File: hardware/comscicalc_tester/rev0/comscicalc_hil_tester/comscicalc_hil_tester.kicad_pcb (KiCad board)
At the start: 4 copper layers, 106 x 61 mm, 116 parts, among them IC1 ADC088S022CIMTX_NOPB, IC2 74HC4052D,653, IC3 74HC4052D,653, IC4 74HC4052D,653, IC5 LM358ADGKR, J1 comscicalc_tester, J2 4-1734839-0, J3 Conn_02x12_Odd_Even, J4 Conn_01x04_Male, J5 Conn_01x02_Male, J6 USB4110-GF-A, Q1 DMG2301L, U1 MCP23017_SS, U2 TLV70033_SOT23-5, U3 RASPBERRY_PI_3_MODEL_B_

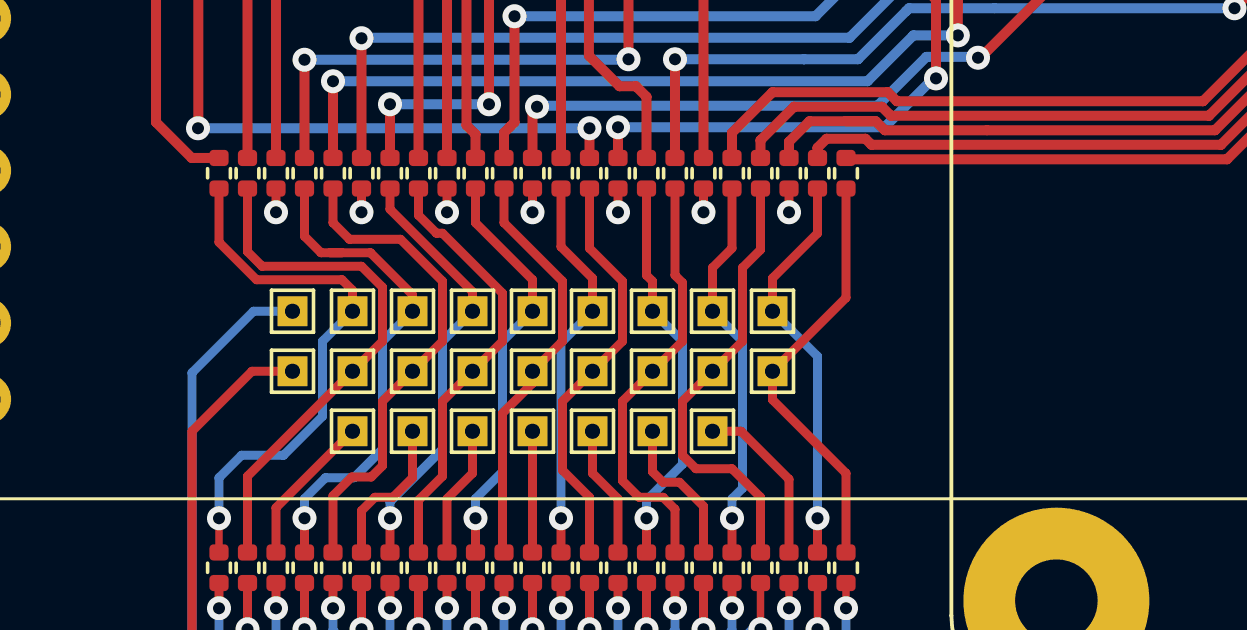
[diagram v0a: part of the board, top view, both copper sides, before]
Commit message: Added some fonts
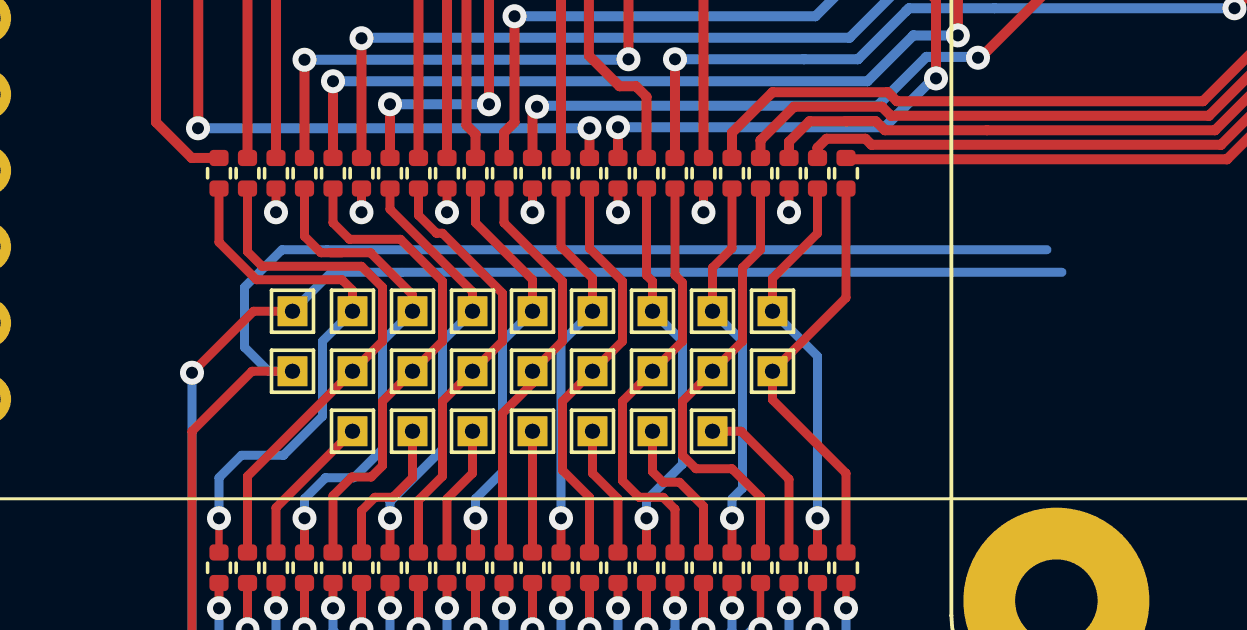
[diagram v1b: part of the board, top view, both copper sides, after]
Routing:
- net BACKLIGHT_FEEDBACK: track 14.8 -> 46.0 mm
- net BACKLIGHT_DRIVE: track 17.0 -> 43.2 mm, vias 0 -> 1
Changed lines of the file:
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@@
   (via (at 129.6425 102.5075) (size 0.8) (drill 0.4) (layers "F.Cu" "B.Cu") (net 3))
   (via (at 73.25 73.195) (size 0.8) (drill 0.4) (layers "F.Cu" "B.Cu") (net 3))
+  (segment (start 78.35 93.3) (end 77.05 93.3) (width 0.3) (layer "F.Cu") (net 30))
+  (segment (start 77.05 93.3) (end 75 95.35) (width 0.3) (layer "F.Cu") (net 30))
+  (via (at 75 95.35) (size 0.8) (drill 0.4) (layers "F.Cu" "B.Cu") (net 30))
   (segment (start 75 104.285718) (end 75 95.35) (width 0.3) (layer "B.Cu") (net 30))
+  (segment (start 78.35 93.3) (end 79.65 92) (width 0.3) (layer "B.Cu") (net 30))
+  (segment (start 82 92) (end 104 92) (width 0.3) (layer "B.Cu") (net 30))
   (segment (start 77.1 107.24856) (end 77.1 106.385718) (width 0.3) (layer "B.Cu") (net 30))
   (segment (start 77.1 106.385718) (end 75 104.285718) (width 0.3) (layer "B.Cu") (net 30))
-  (segment (start 75 95.35) (end 77.05 93.3) (width 0.3) (layer "B.Cu") (net 30))
-  (segment (start 77.05 93.3) (end 78.35 93.3) (width 0.3) (layer "B.Cu") (net 30))
+  (segment (start 79.65 92) (end 82 92) (width 0.3) (layer "B.Cu") (net 30))
   (segment (start 75 105.4) (end 75 97.3) (width 0.3) (layer "F.Cu") (net 31))
   (segment (start 77 95.3) (end 78.35 95.3) (width 0.3) (layer "F.Cu") (net 31))
@@
   (segment (start 76.6 107.24856) (end 76.6 107) (width 0.3) (layer "B.Cu") (net 31))
   (segment (start 76.6 107) (end 75 105.4) (width 0.3) (layer "B.Cu") (net 31))
+  (segment (start 76.75 92.5) (end 78 91.25) (width 0.3) (layer "B.Cu") (net 31))
+  (segment (start 79.5 91.25) (end 103.5 91.25) (width 0.3) (layer "B.Cu") (net 31))
+  (segment (start 78.35 95.3) (end 77.55 95.3) (width 0.3) (layer "B.Cu") (net 31))
+  (segment (start 78 91.25) (end 79.5 91.25) (width 0.3) (layer "B.Cu") (net 31))
+  (segment (start 76.75 94.5) (end 76.75 92.5) (width 0.3) (layer "B.Cu") (net 31))
+  (segment (start 77.55 95.3) (end 76.75 94.5) (width 0.3) (layer "B.Cu") (net 31))
   (segment (start 80.35 93.3) (end 80.35 92.6) (width 0.3) (layer "F.Cu") (net 32))
   (segment (start 75.9 91) (end 75.9 89.21) (width 0.3) (layer "F.Cu") (net 32))
